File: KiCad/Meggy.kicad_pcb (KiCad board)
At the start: 6 copper layers, 17.4 x 54 mm, 27 parts, among them J1 USB_B_Micro, J2 Conn_01x03, Q1 DMP2305U-7, Q2 DMP2305U-7, Q3 DMP2305U-7, SW1 SW_Push, SW2 SW_Push, U1 ROM-socket-42pin, U2 AT90USB1286-MU, U3 M29F160F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

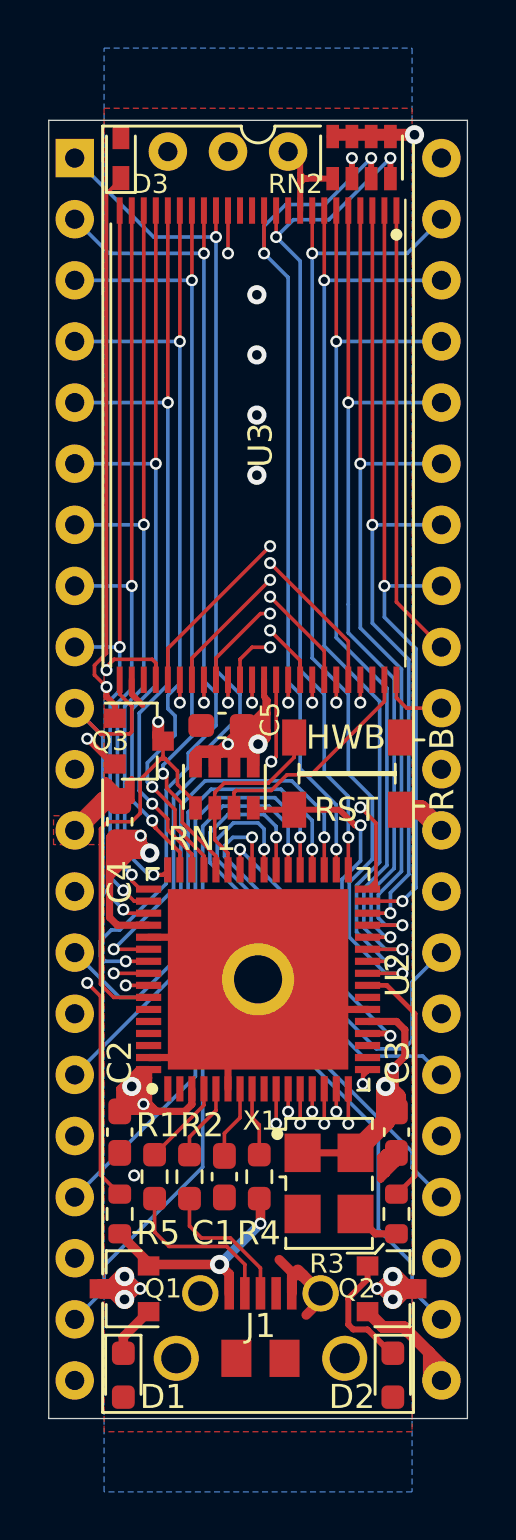
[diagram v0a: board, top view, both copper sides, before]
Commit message: Switched back to 4-layer and did magic routing
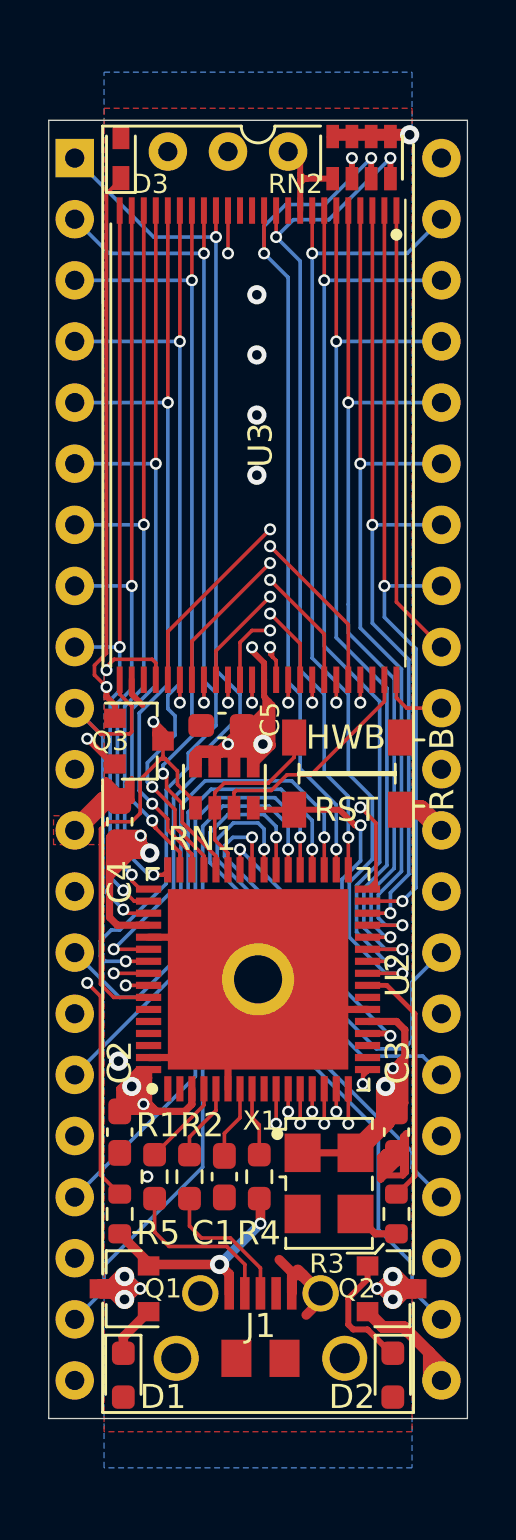
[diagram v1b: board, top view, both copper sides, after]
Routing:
- net BOARD_5V: track 90.1 -> 202.4 mm, vias 15 -> 16
- net A16: track 24.0 -> 32.6 mm
- net D4: track 36.0 -> 42.4 mm
- net D5: track 35.4 -> 40.7 mm
- net D3: track 40.2 -> 45.0 mm
- net GND: track 42.6 -> 47.1 mm, vias 5 -> 6
- net D6: track 33.3 -> 37.1 mm
- net D2: track 39.4 -> 43.2 mm
- net D1: track 39.7 -> 42.9 mm
- net D7: track 37.5 -> 40.3 mm
- net D0: track 43.4 -> 45.8 mm
- net OE_FLASH: track 23.9 -> 25.7 mm
- added copper zone on Inner_signal.Cu, net GND
- removed copper zone on 5V_BOARD, net BOARD_5V
- removed copper zone on GND2, net GND
- removed copper zone on Inner_signal.Cu, net VCC
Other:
- copper layers 6 -> 4

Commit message: Remove Q3 and D3, replace with 74AHCT1G126GW and route OE_SOCKET_EN from pin PE4
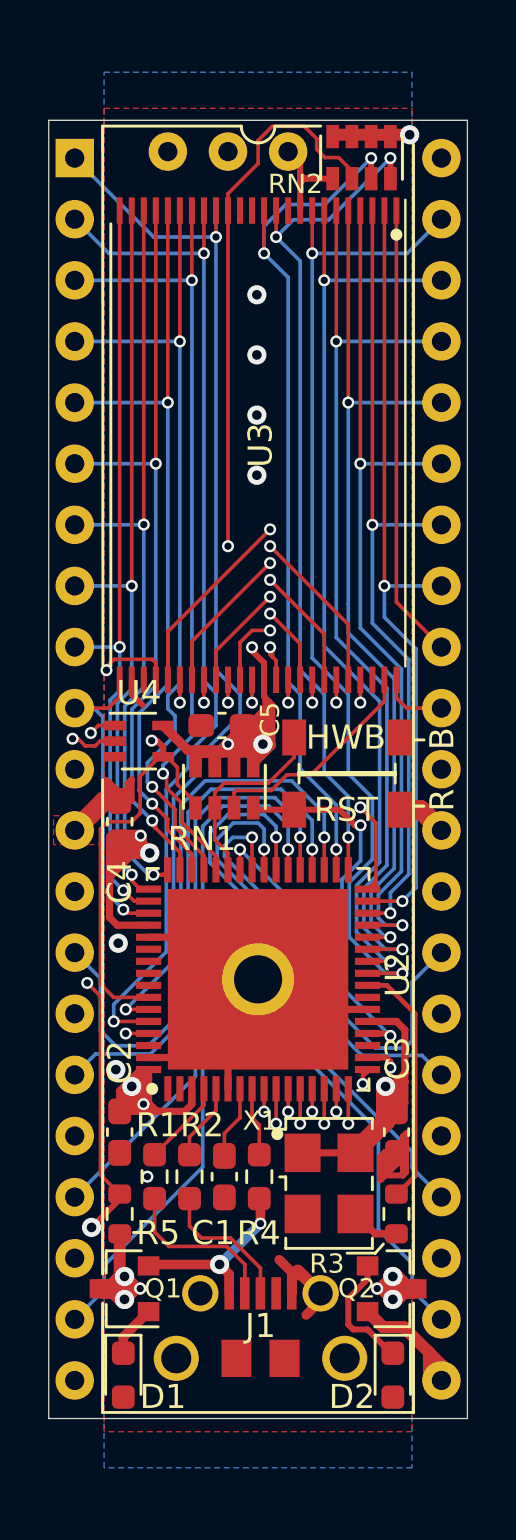
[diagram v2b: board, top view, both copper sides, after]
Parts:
- removed D3: MMDL6050T1G, Diode_SMD:D_SOD-523
- removed Q3: DMP2305U-7, Package_TO_SOT_SMD:SOT-23
- added U4: 74AHCT1G126GW,125, Package_TO_SOT_SMD:SOT-353_SC-70-5, F.Cu at (127.0, 83.1)
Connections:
- R5 pad 1: Net-(D3-Pad1) -> OE_SOCKET_EN
- R5 pad 2: VBUS_5V -> BOARD_5V
- U2 pad 18: /PE4_(NC) -> OE_SOCKET_EN
- U2 pad 54: A18 -> /PF7_(NC)
- U2 pad 55: A17 -> /PF6_(NC)
- U2 pad 56: A16 -> /PF5_(NC)
- U2 pad 57: RY-BY -> /PF4_(NC)
- U2 pad 59: /PF2_(NC) -> A18
- U2 pad 60: /PF1_(NC) -> A17
- U2 pad 61: /PF0_(NC) -> A16
- U2 pad 9: /PE3_(NC) -> RY-BY
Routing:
- net OE_SOCKET_EN: track 0.00 -> 58.5 mm, vias 0 -> 4
- net Net-(D3-Pad1): track 45.6 -> 0.00 mm, vias 2 -> 0
- net RY-BY: track 43.3 -> 52.7 mm, vias 3 -> 2
- net D0: track 45.8 -> 50.2 mm
- net D8: track 26.6 -> 28.9 mm
- net A0: track 15.5 -> 13.6 mm
- net VBUS_5V: track 9.63 -> 7.80 mm
- net A18: track 42.0 -> 43.8 mm
- net A17: track 41.4 -> 43.1 mm
- net OE_SOCKET: track 9.23 -> 10.7 mm
- net A16: track 32.6 -> 31.3 mm
- net D1: track 42.9 -> 44.2 mm
- net OE_FLASH: track 25.7 -> 24.5 mm
- net BOARD_5V: track 202.4 -> 202.3 mm, vias 16 -> 15
- net GND: vias 6 -> 7

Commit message: Fix pin assignments JTAG conflict, power OR circuit, OE isolation
- Replace P-channel MOSFET power OR (Q1/Q2) with Schottky diodes
- Replace Q3 MOSFET OE isolation with 74AHCT1G126GW tristate buffer (PE4 enable, 10k pull-up)
- Move A16/A17/A18 from PF5/PF6/PF7 (JTAG conflict) to PF0/PF1/PF2
- Move RY/BY from PF4 (JTAG conflict) to PE3
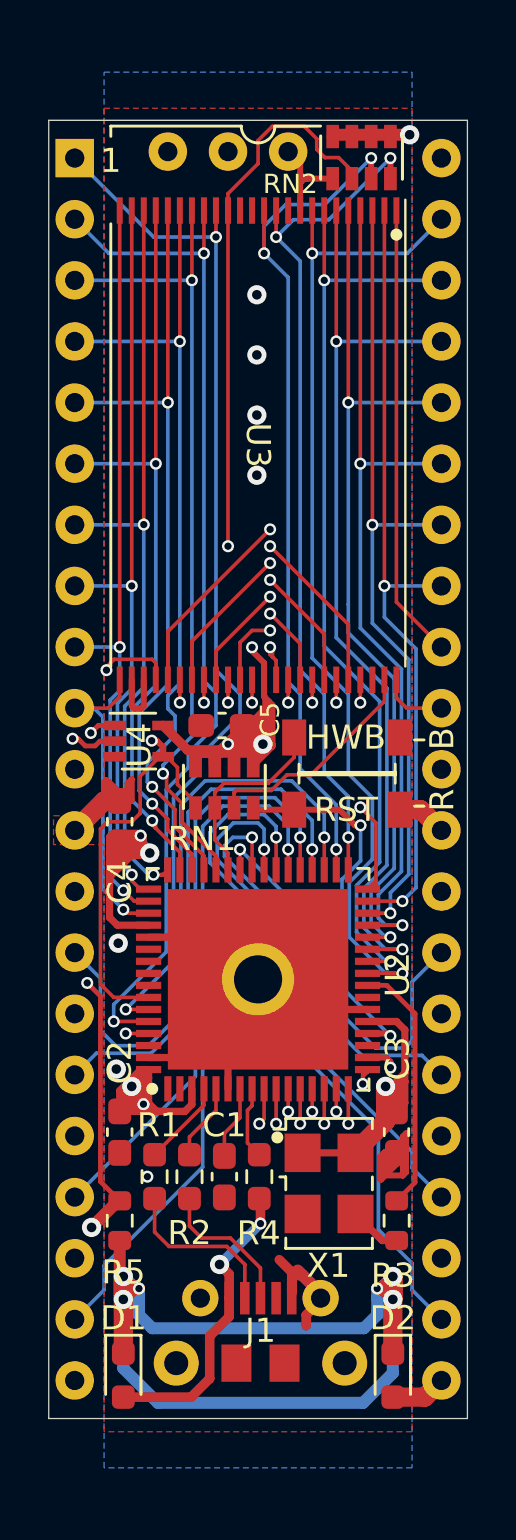
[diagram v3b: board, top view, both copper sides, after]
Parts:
- removed Q1, Q2: DMP2305U-7, Package_TO_SOT_SMD:SOT-23
- D1, D2: value MMDL6050T1G -> CDBU0520
- moved R3 0.28 mm to (137.8, 103.0)
- moved R5 0.28 mm to (126.2, 103.0)
- moved J1 0.20 mm to (132.1, 108.6)
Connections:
- net OE_SOCKET_EN renamed OE_BUF_EN
- D1 pad 1: Net-(D1-Pad1) -> BOARD_5V
- D1 pad 2: GND -> VBUS_5V
- D2 pad 1: Net-(D2-Pad1) -> BOARD_5V
- D2 pad 2: GND -> VCC
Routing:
- net BOARD_5V: track 202.3 -> 219.4 mm
- net Net-(D2-Pad1): track 5.11 -> 0.00 mm
- net VBUS_5V: track 7.80 -> 12.6 mm
- net VCC: track 6.33 -> 2.31 mm
- net Net-(D1-Pad1): track 2.16 -> 0.00 mm
- net GND: track 47.1 -> 49.1 mm
- net RY-BY: track 52.7 -> 53.7 mm
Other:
- board text added: "1MB KS ROM for A500+"
- board text added: "Rev. B Design by J.Bilander (C) 2025,2026"
- board text removed: "1MB KS ROM switch for A500+"
- board text removed: "Rev. A Design by J.Bilander (C) 2025"

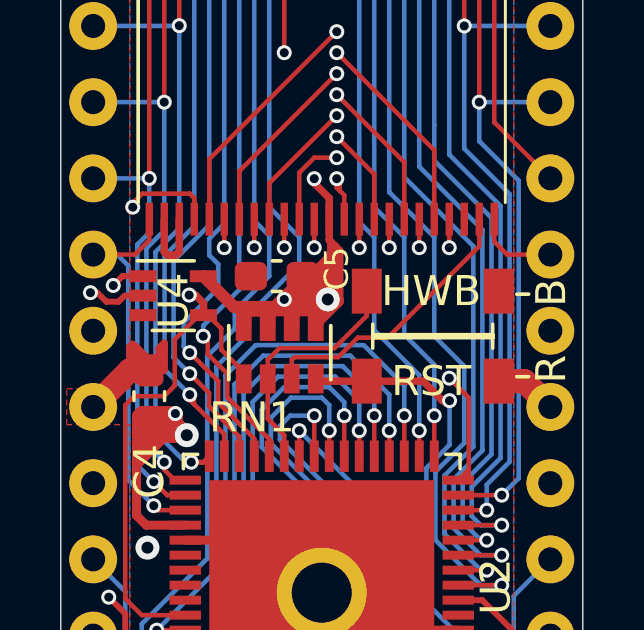
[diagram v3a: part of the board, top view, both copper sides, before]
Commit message: Removed RESET-button
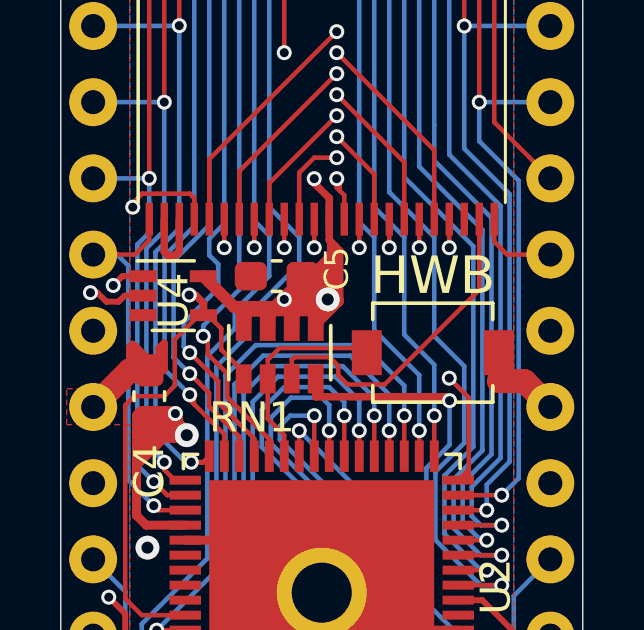
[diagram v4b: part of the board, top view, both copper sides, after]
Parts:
- removed SW2: SW_Push, Meggy:Sunrom_Tactile_Switch_3x4x2mm_SMD_2-Pin
- moved SW1 0.95 mm to (135.7, 85.0)
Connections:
- SW1 pad 2: RESET -> HWB
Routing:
- net BYTE: track 9.36 -> 11.1 mm
- net HWB: track 8.17 -> 6.96 mm
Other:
- board text removed: "B"
- board text removed: "R"
- board text removed: "RST"

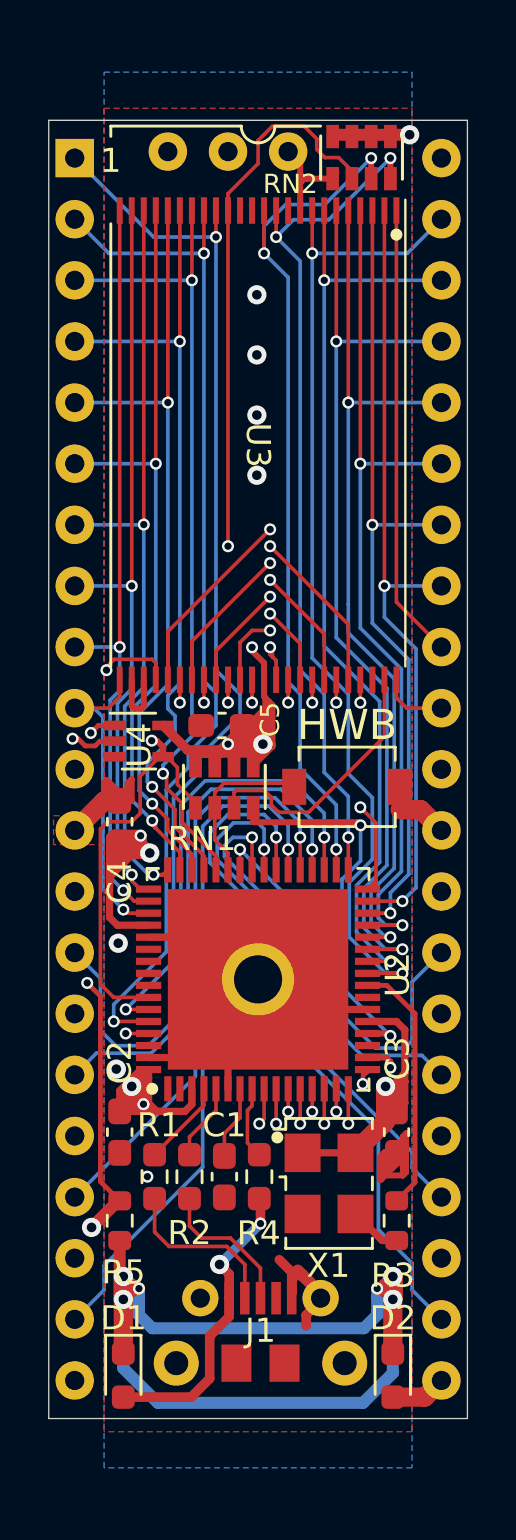
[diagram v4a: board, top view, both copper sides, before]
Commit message: Rev C: connect PE5 (pin 19) to /RESET (pin 20) for software DFU entry via --avr-reset
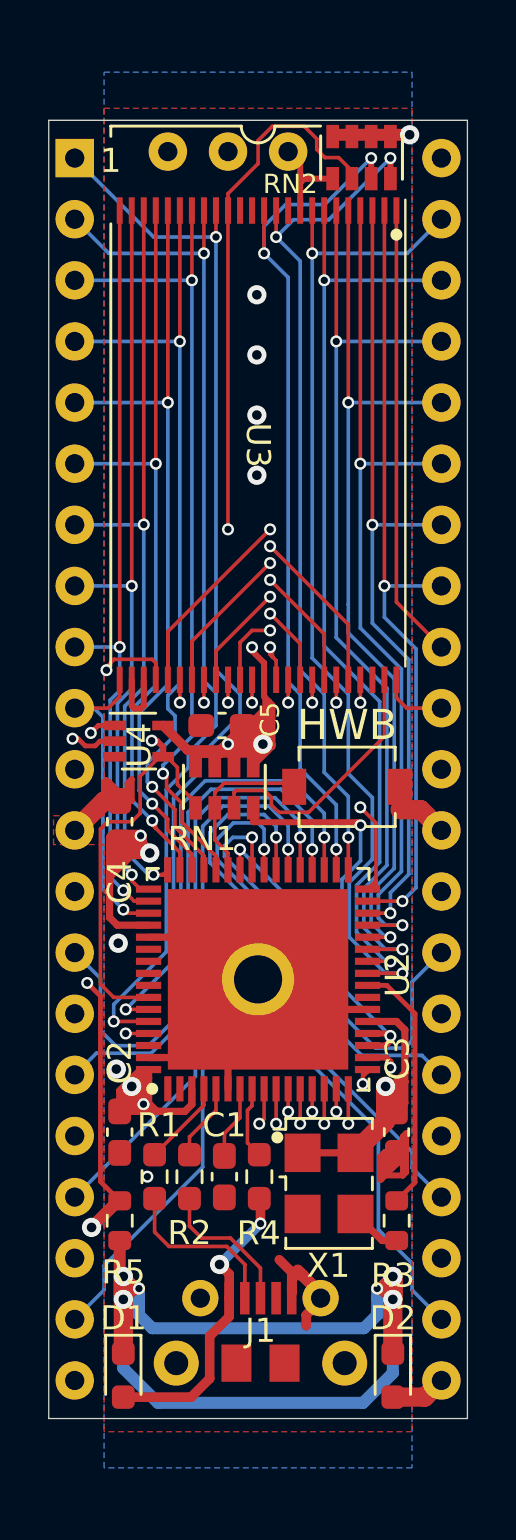
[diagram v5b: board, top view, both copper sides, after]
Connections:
- U2 pad 19: /PE5_(NC) -> RESET
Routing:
- net RESET: track 16.0 -> 17.2 mm
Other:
- board text added: "Rev. C Design by J.Bilander (C) 2025,2026"
- board text removed: "Rev. B Design by J.Bilander (C) 2025,2026"
